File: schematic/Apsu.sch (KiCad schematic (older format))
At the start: 40 parts

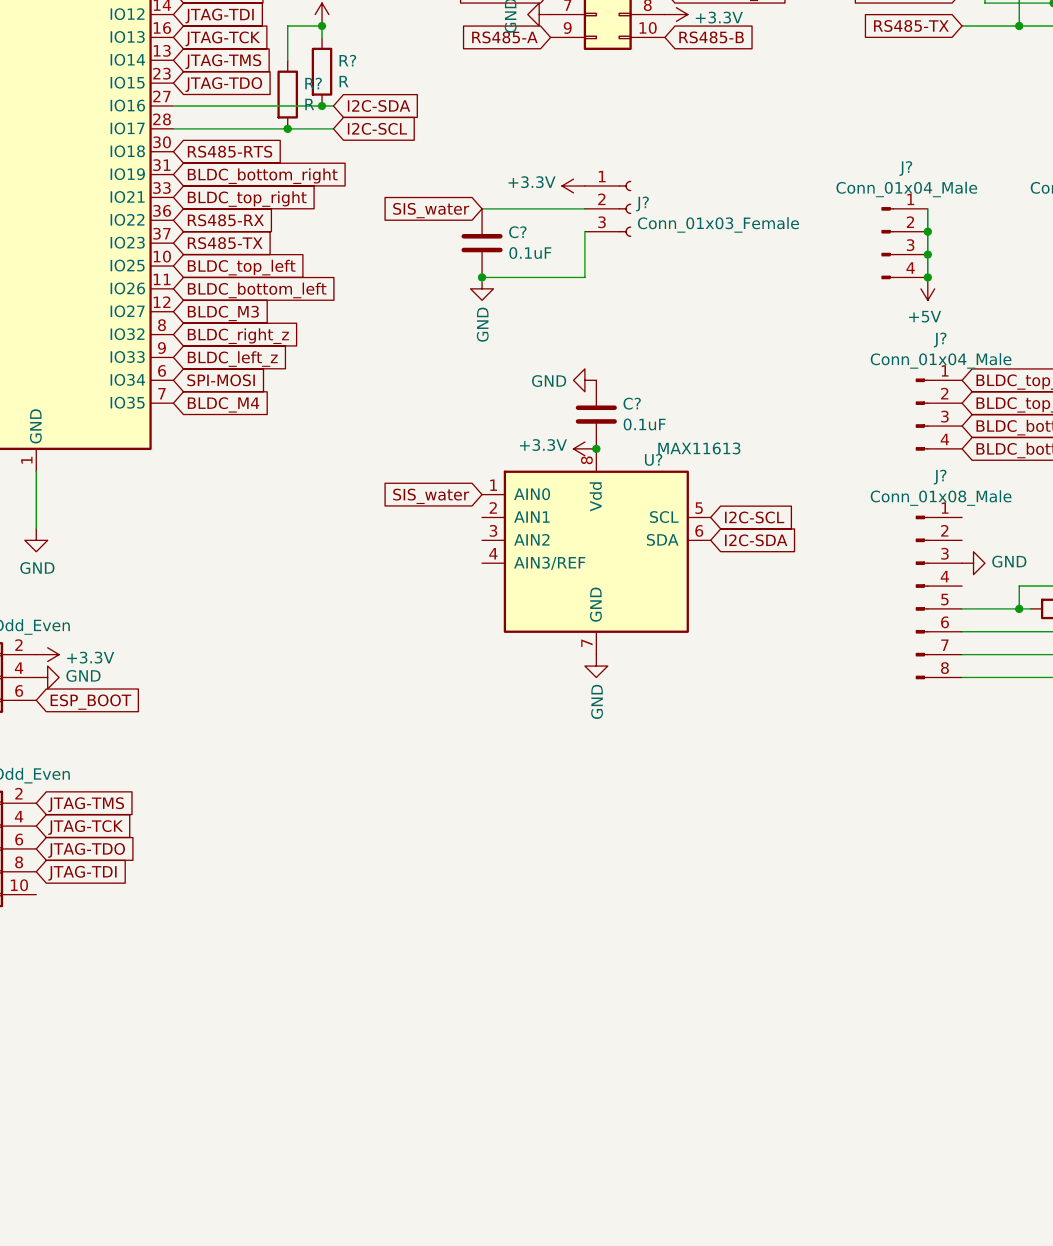
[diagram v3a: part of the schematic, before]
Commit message: SimonK BLDC to I2C -> PWM
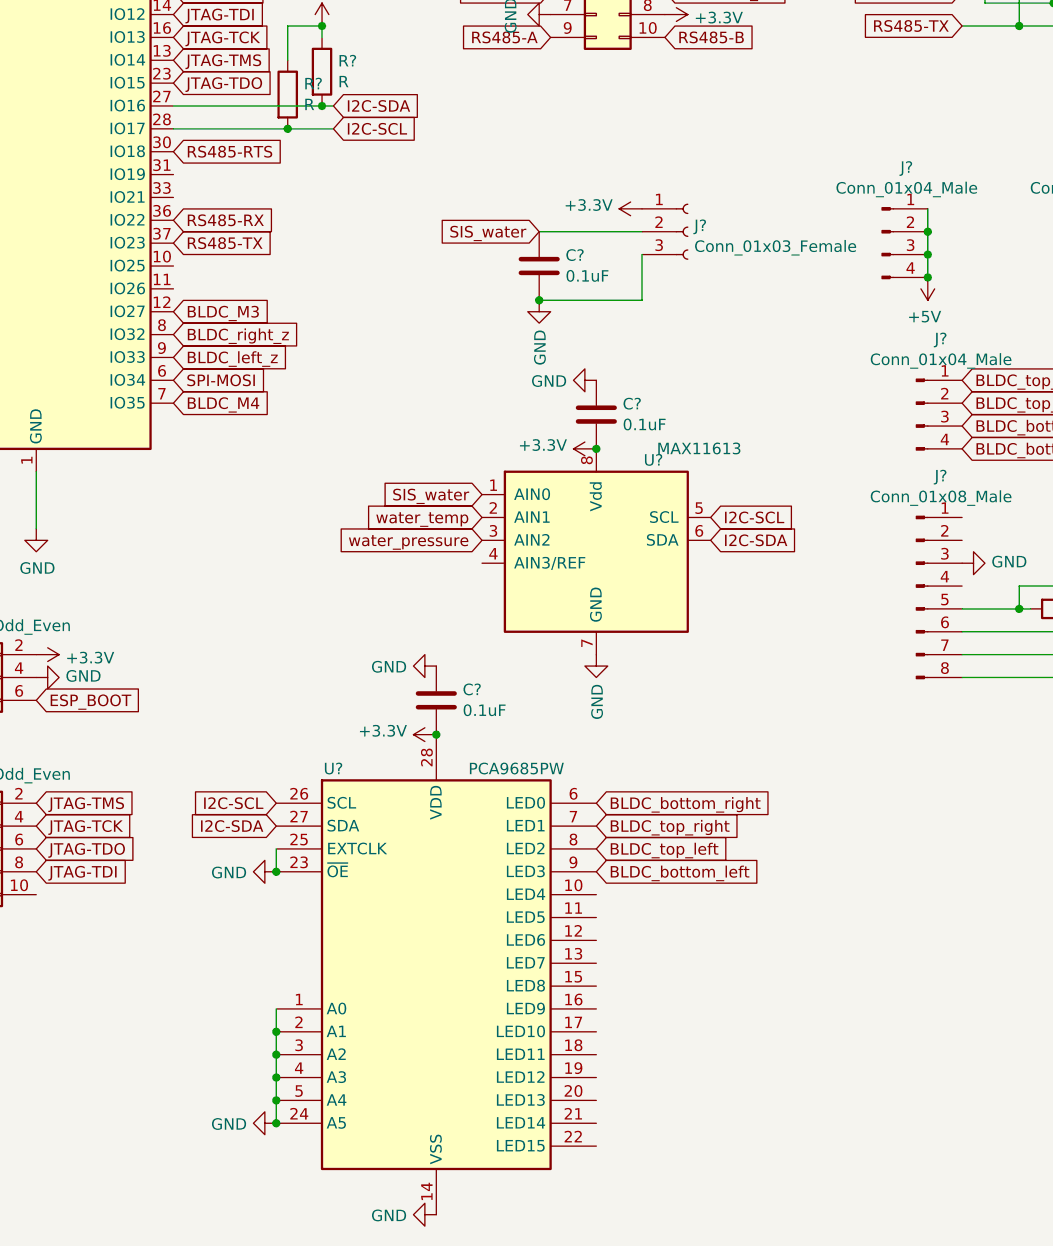
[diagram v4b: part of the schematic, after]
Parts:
- added C?: 0.1uF, symbol Device:C
- added U?: PCA9685PW, Package_SO:TSSOP-28_4.4x9.7mm_P0.65mm, symbol Driver_LED:PCA9685PW
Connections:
- net +3V3: now also C?.2, U?.28 (VDD)
- net BLDC_bottom_left: now also U?.9 (LED3); no longer U?.11 (IO26)
- net BLDC_bottom_right: now also U?.6 (LED0); no longer U?.31 (IO19)
- net BLDC_top_left: now also U?.8 (LED2); no longer U?.10 (IO25)
- net BLDC_top_right: now also U?.7 (LED1); no longer U?.33 (IO21)
- net GND: now also C?.1, U?.1 (A0), U?.14 (VSS), U?.2 (A1), U?.23 (~OE), U?.24 (A5), U?.25 (EXTCLK), U?.3 (A2), U?.4 (A3), U?.5 (A4)
- net I2C-SCL: now also U?.26 (SCL)
- net I2C-SDA: now also U?.27 (SDA)
- net water_temp: now reaches U?.2 (AIN1)
- net water_pressure: now reaches U?.3 (AIN2)
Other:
- moved on the sheet: C?, J?
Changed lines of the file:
@@
 Text GLabel 6450 4250 2    50   Input ~ 0
 BLDC_bottom_right
-Text GLabel 3000 3550 2    50   Input ~ 0
+Text GLabel 4850 6100 2    50   Input ~ 0
 BLDC_bottom_left
-Text GLabel 3000 3450 2    50   Input ~ 0
+Text GLabel 4850 6000 2    50   Input ~ 0
 BLDC_top_left
-Text GLabel 3000 3050 2    50   Input ~ 0
+Text GLabel 4850 5800 2    50   Input ~ 0
 BLDC_bottom_right
-Text GLabel 3000 3150 2    50   Input ~ 0
+Text GLabel 4850 5900 2    50   Input ~ 0
 BLDC_top_right
 Text GLabel 3000 3850 2    50   Input ~ 0
@@
 Wire Wire Line
 	7450 5050 8200 5050
-Text GLabel 4350 3200 0    50   Input ~ 0
+Text GLabel 4600 3300 0    50   Input ~ 0
 SIS_water
 $Comp
 L Connector:Conn_01x03_Female J?
 U 1 1 5ECCBC75
-P 5000 3200
-F 0 "J?" H 5028 3226 50  0000 L CNN
-F 1 "Conn_01x03_Female" H 5028 3135 50  0000 L CNN
-F 2 "" H 5000 3200 50  0001 C CNN
-F 3 "~" H 5000 3200 50  0001 C CNN
-	1    5000 3200
+P 5250 3300
+F 0 "J?" H 5278 3326 50  0000 L CNN
+F 1 "Conn_01x03_Female" H 5278 3235 50  0000 L CNN
+F 2 "" H 5250 3300 50  0001 C CNN
+F 3 "~" H 5250 3300 50  0001 C CNN
+	1    5250 3300
 	1    0    0    -1
 $EndComp
@@
 L power:+3.3V #PWR?
 U 1 1 5ECD2BAF
-P 4800 3100
-F 0 "#PWR?" H 4800 2950 50  0001 C CNN
-F 1 "+3.3V" V 4815 3228 50  0000 L CNN
-F 2 "" H 4800 3100 50  0001 C CNN
-F 3 "" H 4800 3100 50  0001 C CNN
-	1    4800 3100
+P 5050 3200
+F 0 "#PWR?" H 5050 3050 50  0001 C CNN
+F 1 "+3.3V" V 5065 3328 50  0000 L CNN
+F 2 "" H 5050 3200 50  0001 C CNN
+F 3 "" H 5050 3200 50  0001 C CNN
+	1    5050 3200
 	0    -1   -1   0
 $EndComp
@@
 L power:GND #PWR?
 U 1 1 5ECD5B58
-P 4350 3500
-F 0 "#PWR?" H 4350 3250 50  0001 C CNN
-F 1 "GND" V 4355 3372 50  0000 R CNN
-F 2 "" H 4350 3500 50  0001 C CNN
-F 3 "" H 4350 3500 50  0001 C CNN
-	1    4350 3500
+P 4600 3600
+F 0 "#PWR?" H 4600 3350 50  0001 C CNN
+F 1 "GND" V 4605 3472 50  0000 R CNN
+F 2 "" H 4600 3600 50  0001 C CNN
+F 3 "" H 4600 3600 50  0001 C CNN
+	1    4600 3600
 	1    0    0    -1
 $EndComp
@@
 L Device:C C?
 U 1 1 5EC9474D
-P 4350 3350
-F 0 "C?" H 4465 3396 50  0000 L CNN
-F 1 "0.1uF" H 4465 3305 50  0000 L CNN
-F 2 "" H 4388 3200 50  0001 C CNN
-F 3 "~" H 4350 3350 50  0001 C CNN
-	1    4350 3350
-	1    0    0    -1
-$EndComp
-Wire Wire Line
-	4800 3200 4350 3200
-Wire Wire Line
-	4350 3500 4800 3500
-Wire Wire Line
-	4800 3500 4800 3300
-Connection ~ 4350 3500
+P 4600 3450
+F 0 "C?" H 4715 3496 50  0000 L CNN
+F 1 "0.1uF" H 4715 3405 50  0000 L CNN
+F 2 "" H 4638 3300 50  0001 C CNN
+F 3 "~" H 4600 3450 50  0001 C CNN
+	1    4600 3450
+	1    0    0    -1
+$EndComp
+Wire Wire Line
+	5050 3300 4600 3300
+Wire Wire Line
+	4600 3600 5050 3600
+Wire Wire Line
+	5050 3600 5050 3400
+Connection ~ 4600 3600
 $Comp
 L RF_Module:ESP32-WROOM-32 U?
@@
 	6300 3300 6300 3200
 Connection ~ 6300 3300
-$Comp
-L Analog_ADC:MAX11613 U?
-U 1 1 5EC93959
-P 4850 4650
-F 0 "U?" H 5100 5000 50  0000 C CNN
-F 1 "MAX11613" H 5300 5050 50  0000 C CNN
-F 2 "Package_SO:MSOP-8_3x3mm_P0.65mm" H 5300 4300 50  0001 L CNN
-F 3 "https://datasheets.maximintegrated.com/en/ds/MAX11612-MAX11617.pdf" H 4950 5150 50  0001 C CNN
-	1    4850 4650
-	1    0    0    -1
-$EndComp
 Text GLabel 4350 4450 0    50   Input ~ 0
 SIS_water
@@
 	1    4850 5150
 	1    0    0    -1
-$EndComp
-$Comp
-L power:+3.3V #PWR?
-U 1 1 5EC9658D
-P 4850 4250
-F 0 "#PWR?" H 4850 4100 50  0001 C CNN
-F 1 "+3.3V" V 4865 4378 50  0000 L CNN
-F 2 "" H 4850 4250 50  0001 C CNN
-F 3 "" H 4850 4250 50  0001 C CNN
-	1    4850 4250
-	0    -1   -1   0
 $EndComp
 $Comp
@@
 Wire Wire Line
 	3500 2850 3700 2850
-$Comp
-L Device:C C?
-U 1 1 5ECDE2A9
-P 4850 4100
-F 0 "C?" H 4965 4146 50  0000 L CNN
-F 1 "0.1uF" H 4965 4055 50  0000 L CNN
-F 2 "" H 4888 3950 50  0001 C CNN
-F 3 "~" H 4850 4100 50  0001 C CNN
-	1    4850 4100
-	1    0    0    -1
-$EndComp
-Connection ~ 4850 4250
-$Comp
-L power:GND #PWR?
-U 1 1 5ECDF4E3
-P 4850 3950
-F 0 "#PWR?" H 4850 3700 50  0001 C CNN
-F 1 "GND" V 4855 3822 50  0000 R CNN
-F 2 "" H 4850 3950 50  0001 C CNN
-F 3 "" H 4850 3950 50  0001 C CNN
-	1    4850 3950
-	0    1    1    0
-$EndComp
 $Comp
 L power:+3.3V #PWR?
@@
 Text GLabel 5150 2250 2    50   Input ~ 0
 SPI-UART_SS
+Text GLabel 4350 4550 0    50   Input ~ 0
+water_temp
+Text GLabel 4350 4650 0    50   Input ~ 0
+water_pressure
+$Comp
+L Driver_LED:PCA9685PW U?
+U 1 1 5ED4A7C9
+P 4150 6500
+F 0 "U?" H 3700 7350 50  0000 C CNN
+F 1 "PCA9685PW" H 4500 7350 50  0000 C CNN
+F 2 "Package_SO:TSSOP-28_4.4x9.7mm_P0.65mm" H 4175 5525 50  0001 L CNN
+F 3 "http://www.nxp.com/documents/data_sheet/PCA9685.pdf" H 3750 7200 50  0001 C CNN
+	1    4150 6500
+	1    0    0    -1
+$EndComp
+Text GLabel 3450 5800 0    50   Input ~ 0
+I2C-SCL
+Text GLabel 3450 5900 0    50   Input ~ 0
+I2C-SDA
+Connection ~ 4850 4250
+$Comp
+L power:+3.3V #PWR?
+U 1 1 5EC9658D
+P 4850 4250
+F 0 "#PWR?" H 4850 4100 50  0001 C CNN
+F 1 "+3.3V" V 4865 4378 50  0000 L CNN
+F 2 "" H 4850 4250 50  0001 C CNN
+F 3 "" H 4850 4250 50  0001 C CNN
+	1    4850 4250
+	0    -1   -1   0
+$EndComp
+$Comp
+L Device:C C?
+U 1 1 5ECDE2A9
+P 4850 4100
+F 0 "C?" H 4965 4146 50  0000 L CNN
+F 1 "0.1uF" H 4965 4055 50  0000 L CNN
+F 2 "" H 4888 3950 50  0001 C CNN
+F 3 "~" H 4850 4100 50  0001 C CNN
+	1    4850 4100
+	1    0    0    -1
+$EndComp
+$Comp
+L Analog_ADC:MAX11613 U?
+U 1 1 5EC93959
+P 4850 4650
+F 0 "U?" H 5100 5000 50  0000 C CNN
+F 1 "MAX11613" H 5300 5050 50  0000 C CNN
+F 2 "Package_SO:MSOP-8_3x3mm_P0.65mm" H 5300 4300 50  0001 L CNN
+F 3 "https://datasheets.maximintegrated.com/en/ds/MAX11612-MAX11617.pdf" H 4950 5150 50  0001 C CNN
+	1    4850 4650
+	1    0    0    -1
+$EndComp
+$Comp
+L power:+3.3V #PWR?
+U 1 1 5ED6EBD3
+P 4150 5500
+F 0 "#PWR?" H 4150 5350 50  0001 C CNN
+F 1 "+3.3V" V 4165 5628 50  0000 L CNN
+F 2 "" H 4150 5500 50  0001 C CNN
+F 3 "" H 4150 5500 50  0001 C CNN
+	1    4150 5500
+	0    -1   -1   0
+$EndComp
+$Comp
+L Device:C C?
+U 1 1 5ED70499
+P 4150 5350
+F 0 "C?" H 4265 5396 50  0000 L CNN
+F 1 "0.1uF" H 4265 5305 50  0000 L CNN
+F 2 "" H 4188 5200 50  0001 C CNN
+F 3 "~" H 4150 5350 50  0001 C CNN
+	1    4150 5350
+	1    0    0    -1
+$EndComp
+Connection ~ 4150 5500
+$Comp
+L power:GND #PWR?
+U 1 1 5ECDF4E3
+P 4850 3950
+F 0 "#PWR?" H 4850 3700 50  0001 C CNN
+F 1 "GND" V 4855 3822 50  0000 R CNN
+F 2 "" H 4850 3950 50  0001 C CNN
+F 3 "" H 4850 3950 50  0001 C CNN
+	1    4850 3950
+	0    1    1    0
+$EndComp
+$Comp
+L power:GND #PWR?
+U 1 1 5ED71C84
+P 4150 5200
+F 0 "#PWR?" H 4150 4950 50  0001 C CNN
+F 1 "GND" V 4155 5072 50  0000 R CNN
+F 2 "" H 4150 5200 50  0001 C CNN
+F 3 "" H 4150 5200 50  0001 C CNN
+	1    4150 5200
+	0    1    1    0
+$EndComp
+$Comp
+L power:GND #PWR?
+U 1 1 5ED7E0CA
+P 4150 7600
+F 0 "#PWR?" H 4150 7350 50  0001 C CNN
+F 1 "GND" V 4155 7472 50  0000 R CNN
+F 2 "" H 4150 7600 50  0001 C CNN
+F 3 "" H 4150 7600 50  0001 C CNN
+	1    4150 7600
+	0    1    1    0
+$EndComp
+Wire Wire Line
+	3450 6000 3450 6100
+Wire Wire Line
+	3450 6700 3450 6800
+Wire Wire Line
+	3450 6800 3450 6900
+Connection ~ 3450 6800
+Wire Wire Line
+	3450 6900 3450 7000
+Connection ~ 3450 6900
+Wire Wire Line
+	3450 7000 3450 7100
+Connection ~ 3450 7000
+Wire Wire Line
+	3450 7100 3450 7200
+Connection ~ 3450 7100
+$Comp
+L power:GND #PWR?
+U 1 1 5ED9BD45
+P 3450 7200
+F 0 "#PWR?" H 3450 6950 50  0001 C CNN
+F 1 "GND" V 3455 7072 50  0000 R CNN
+F 2 "" H 3450 7200 50  0001 C CNN
+F 3 "" H 3450 7200 50  0001 C CNN
+	1    3450 7200
+	0    1    1    0
+$EndComp
+Connection ~ 3450 7200
+$Comp
+L power:GND #PWR?
+U 1 1 5ED9C14C
+P 3450 6100
+F 0 "#PWR?" H 3450 5850 50  0001 C CNN
+F 1 "GND" V 3455 5972 50  0000 R CNN
+F 2 "" H 3450 6100 50  0001 C CNN
+F 3 "" H 3450 6100 50  0001 C CNN
+	1    3450 6100
+	0    1    1    0
+$EndComp
+Connection ~ 3450 6100
 $EndSCHEMATC

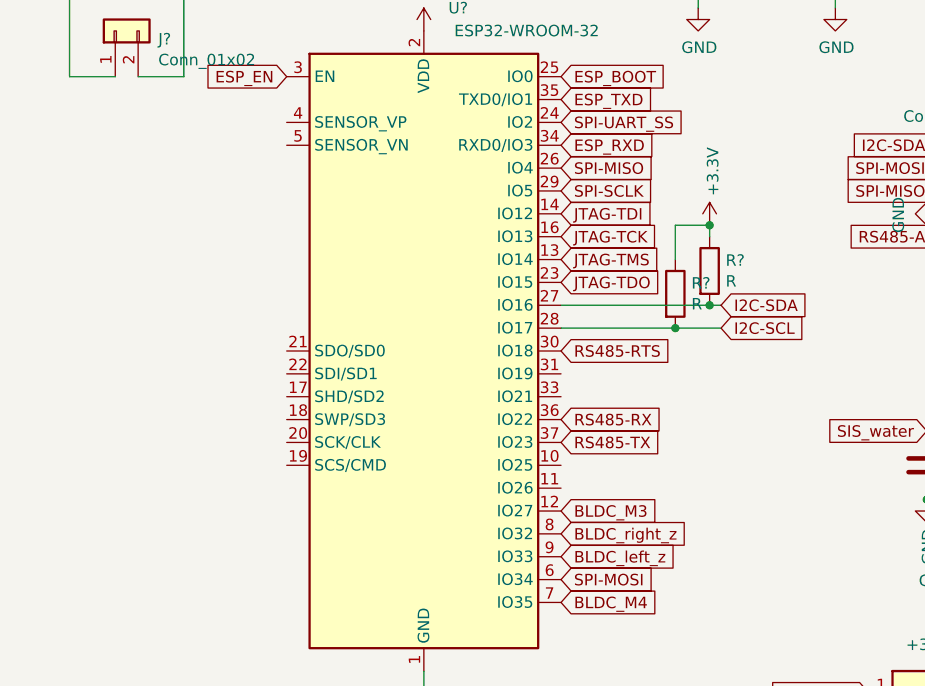
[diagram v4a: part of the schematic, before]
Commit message: added DS18B20 conn
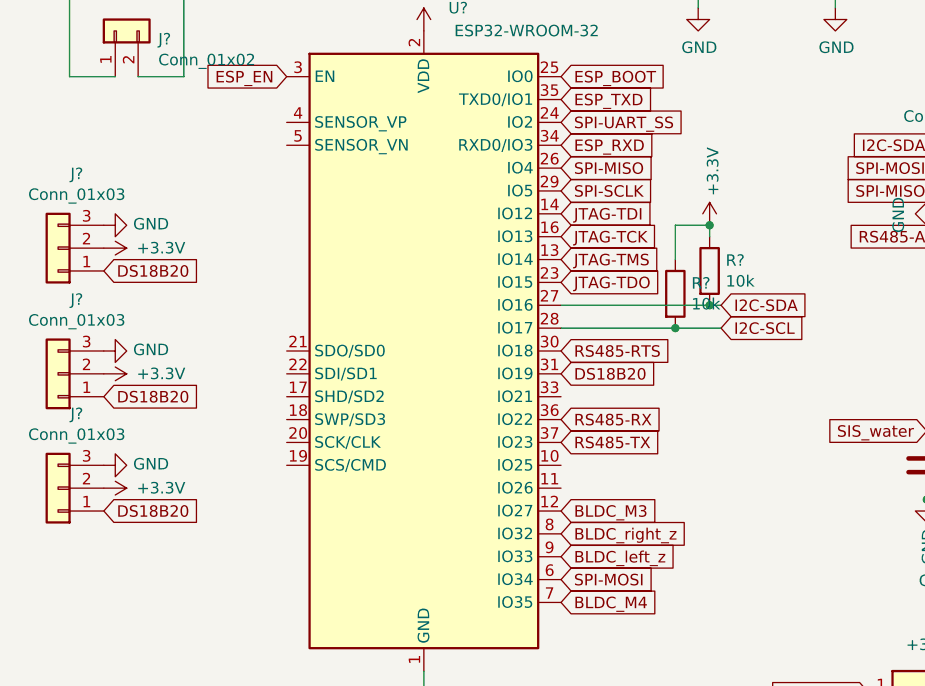
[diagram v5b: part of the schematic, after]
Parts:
- added J? (x3): Conn_01x03, symbol Connector_Generic:Conn_01x03
- R? (x2): value R -> 10k
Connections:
- net +3V3: now also J?.2 (Pin_2), J?.2 (Pin_2), J?.2 (Pin_2)
- net GND: now also J?.3 (Pin_3), J?.3 (Pin_3), J?.3 (Pin_3)
- net DS18B20: now reaches U?.31 (IO19)
- net DS18B20: now also J?.1 (Pin_1), J?.1 (Pin_1), J?.1 (Pin_1)
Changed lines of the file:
@@
 P 3500 2700
 F 0 "R?" H 3570 2746 50  0000 L CNN
-F 1 "R" H 3570 2655 50  0000 L CNN
+F 1 "10k" H 3570 2655 50  0000 L CNN
 F 2 "" V 3430 2700 50  0001 C CNN
 F 3 "~" H 3500 2700 50  0001 C CNN
@@
 P 3650 2600
 F 0 "R?" H 3720 2646 50  0000 L CNN
-F 1 "R" H 3720 2555 50  0000 L CNN
+F 1 "10k" H 3720 2555 50  0000 L CNN
 F 2 "" V 3580 2600 50  0001 C CNN
 F 3 "~" H 3650 2600 50  0001 C CNN
@@
 $EndComp
 Connection ~ 3450 6100
+Text GLabel 3000 3050 2    50   Input ~ 0
+DS18B20
+$Comp
+L Connector_Generic:Conn_01x03 J?
+U 1 1 5EDE12D5
+P 800 2500
+F 0 "J?" H 718 2175 50  0000 C CNN
+F 1 "Conn_01x03" H 718 2266 50  0000 C CNN
+F 2 "" H 800 2500 50  0001 C CNN
+F 3 "~" H 800 2500 50  0001 C CNN
+	1    800  2500
+	-1   0    0    1
+$EndComp
+Text GLabel 1000 2600 2    50   Input ~ 0
+DS18B20
+$Comp
+L power:+3.3V #PWR?
+U 1 1 5EDE39FE
+P 1000 2500
+F 0 "#PWR?" H 1000 2350 50  0001 C CNN
+F 1 "+3.3V" V 1000 2750 50  0000 C CNN
+F 2 "" H 1000 2500 50  0001 C CNN
+F 3 "" H 1000 2500 50  0001 C CNN
+	1    1000 2500
+	0    1    1    0
+$EndComp
+$Comp
+L power:GND #PWR?
+U 1 1 5EDE5749
+P 1000 2400
+F 0 "#PWR?" H 1000 2150 50  0001 C CNN
+F 1 "GND" V 1005 2272 50  0000 R CNN
+F 2 "" H 1000 2400 50  0001 C CNN
+F 3 "" H 1000 2400 50  0001 C CNN
+	1    1000 2400
+	0    -1   -1   0
+$EndComp
+$Comp
+L Connector_Generic:Conn_01x03 J?
+U 1 1 5EDF003B
+P 800 3050
+F 0 "J?" H 718 2725 50  0000 C CNN
+F 1 "Conn_01x03" H 718 2816 50  0000 C CNN
+F 2 "" H 800 3050 50  0001 C CNN
+F 3 "~" H 800 3050 50  0001 C CNN
+	1    800  3050
+	-1   0    0    1
+$EndComp
+Text GLabel 1000 3150 2    50   Input ~ 0
+DS18B20
+$Comp
+L power:+3.3V #PWR?
+U 1 1 5EDF0046
+P 1000 3050
+F 0 "#PWR?" H 1000 2900 50  0001 C CNN
+F 1 "+3.3V" V 1000 3300 50  0000 C CNN
+F 2 "" H 1000 3050 50  0001 C CNN
+F 3 "" H 1000 3050 50  0001 C CNN
+	1    1000 3050
+	0    1    1    0
+$EndComp
+$Comp
+L power:GND #PWR?
+U 1 1 5EDF0050
+P 1000 2950
+F 0 "#PWR?" H 1000 2700 50  0001 C CNN
+F 1 "GND" V 1005 2822 50  0000 R CNN
+F 2 "" H 1000 2950 50  0001 C CNN
+F 3 "" H 1000 2950 50  0001 C CNN
+	1    1000 2950
+	0    -1   -1   0
+$EndComp
+$Comp
+L Connector_Generic:Conn_01x03 J?
+U 1 1 5EDF6F63
+P 800 3550
+F 0 "J?" H 718 3225 50  0000 C CNN
+F 1 "Conn_01x03" H 718 3316 50  0000 C CNN
+F 2 "" H 800 3550 50  0001 C CNN
+F 3 "~" H 800 3550 50  0001 C CNN
+	1    800  3550
+	-1   0    0    1
+$EndComp
+Text GLabel 1000 3650 2    50   Input ~ 0
+DS18B20
+$Comp
+L power:+3.3V #PWR?
+U 1 1 5EDF6F6E
+P 1000 3550
+F 0 "#PWR?" H 1000 3400 50  0001 C CNN
+F 1 "+3.3V" V 1000 3800 50  0000 C CNN
+F 2 "" H 1000 3550 50  0001 C CNN
+F 3 "" H 1000 3550 50  0001 C CNN
+	1    1000 3550
+	0    1    1    0
+$EndComp
+$Comp
+L power:GND #PWR?
+U 1 1 5EDF6F78
+P 1000 3450
+F 0 "#PWR?" H 1000 3200 50  0001 C CNN
+F 1 "GND" V 1005 3322 50  0000 R CNN
+F 2 "" H 1000 3450 50  0001 C CNN
+F 3 "" H 1000 3450 50  0001 C CNN
+	1    1000 3450
+	0    -1   -1   0
+$EndComp
 $EndSCHEMATC
